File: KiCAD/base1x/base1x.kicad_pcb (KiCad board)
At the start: 4 copper layers, 62.2 x 110 mm, 39 parts, among them J1 Conn_02x05_Odd_Even, J2 GS3, J3 Conn_02x14_Counter_Clockwise, J4 GS3, J6 Conn_02x14_Counter_Clockwise, J7 Conn_02x06_Counter_Clockwise, J8 Conn_02x06_Counter_Clockwise, J9 Screw_Terminal_01x08, P3 CONN_01X02, P4 CONN_01X02, U1 ADS1115

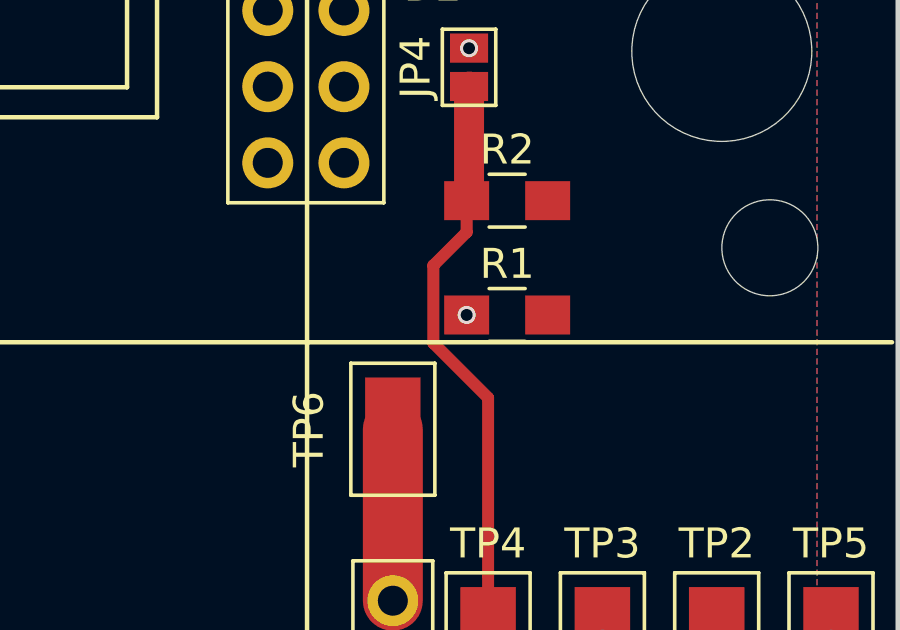
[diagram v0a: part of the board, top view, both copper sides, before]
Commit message: fix some clearance issues on base1x
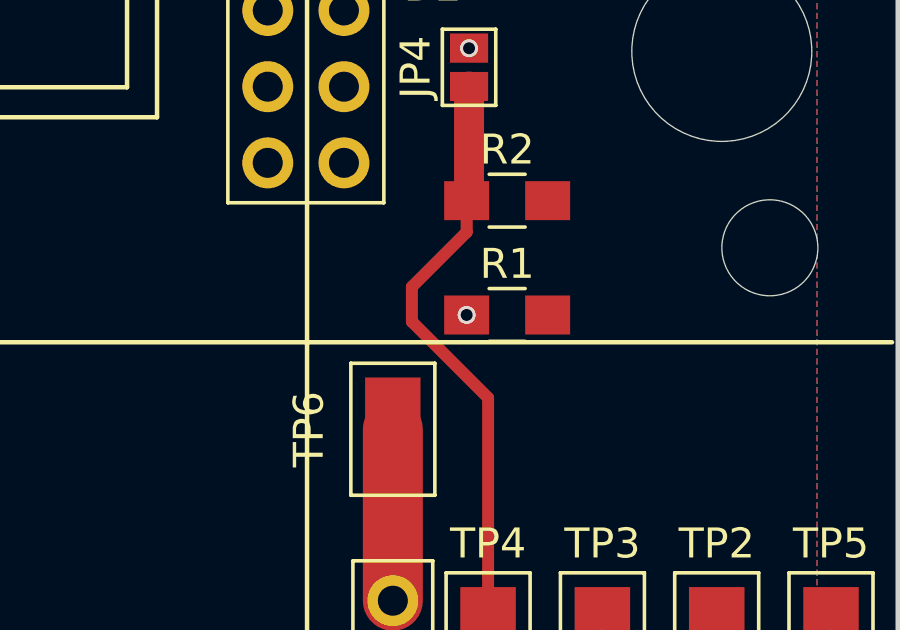
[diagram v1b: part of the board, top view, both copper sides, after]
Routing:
- net Net-(JP4-Pad1): track 26.3 -> 26.8 mm
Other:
- net class Default: clearance 0.16 -> 0.17
- rule trace_clearance: 0.16 -> 0.17
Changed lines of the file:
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@@
     (thickness 1.6)
     (drawings 27)
-    (tracks 210)
+    (tracks 214)
     (zones 0)
     (modules 39)
@@
     (user_trace_width 1)
     (user_trace_width 2)
-    (trace_clearance 0.16)
+    (trace_clearance 0.17)
     (zone_clearance 0.17)
     (zone_45_only no)
@@
   (net 28 "Net-(D2-Pad2)")
   (net_class Default "This is the default net class."
-    (clearance 0.16)
+    (clearance 0.17)
     (trace_width 0.25)
     (via_dia 0.6)
@@
   (segment (start -21.27 -1.26) (end -18.73 -1.26) (width 1) (layer In1.Cu) (net 1))
   (segment (start 21.23 -1.26) (end 18.69 -1.26) (width 1) (layer In1.Cu) (net 1))
+  (segment (start -8.075736 5.020001) (end -8.065736 5.030001) (width 0.4) (layer In1.Cu) (net 3))
+  (segment (start -8.5 5.020001) (end -8.075736 5.020001) (width 0.4) (layer In1.Cu) (net 3))
+  (segment (start -8.065736 5.030001) (end 17.479999 5.030001) (width 0.4) (layer In1.Cu) (net 3))
+  (segment (start 17.479999 5.030001) (end 17.840001 4.669999) (width 0.4) (layer In1.Cu) (net 3))
+  (segment (start 17.840001 4.669999) (end 18.69 3.82) (width 0.4) (layer In1.Cu) (net 3))
+  (segment (start -4.680001 -47.231997) (end -4.680001 -49.579999) (width 0.4) (layer In2.Cu) (net 4))
+  (segment (start -4.680001 -49.579999) (end -4.309999 -49.950001) (width 0.4) (layer In2.Cu) (net 4))
+  (segment (start -9.525 -42.386998) (end -4.680001 -47.231997) (width 0.4) (layer In2.Cu) (net 4))
+  (segment (start -4.309999 -49.950001) (end -3.46 -50.8) (width 0.4) (layer In2.Cu) (net 4))
   (segment (start -9.525 1.27) (end -9.525 -42.386998) (width 0.4) (layer In2.Cu) (net 4))
-  (segment (start -9.525 -42.386998) (end -9.366998 -42.545) (width 0.4) (layer In2.Cu) (net 4))
   (segment (start 18.69 1.28) (end -9.535 1.28) (width 1) (layer In1.Cu) (net 4))
   (segment (start -9.535 1.28) (end -9.525 1.27) (width 1) (layer In1.Cu) (net 4))
@@
   (segment (start -21.27 1.28) (end -18.73 1.28) (width 1) (layer In1.Cu) (net 4))
   (segment (start 21.23 1.28) (end 18.69 1.28) (width 1) (layer In1.Cu) (net 4))
+  (segment (start 27.305 25.4) (end 23.495 21.59) (width 0.4) (layer In2.Cu) (net 6))
+  (segment (start 27.305 38.1) (end 27.305 25.4) (width 0.4) (layer In2.Cu) (net 6))
+  (segment (start 22.079999 -8.030001) (end 21.23 -8.88) (width 0.4) (layer In2.Cu) (net 6))
+  (segment (start 23.495 21.59) (end 23.495 -6.615) (width 0.4) (layer In2.Cu) (net 6))
+  (segment (start 23.495 -6.615) (end 22.079999 -8.030001) (width 0.4) (layer In2.Cu) (net 6))
+  (segment (start 1.62 -9.165) (end 1.905 -8.88) (width 0.4) (layer In2.Cu) (net 6))
+  (segment (start 1.62 -48.26) (end 1.62 -9.165) (width 0.4) (layer In2.Cu) (net 6))
+  (segment (start 2.840001 -13.054999) (end 2.840001 -49.579999) (width 0.4) (layer In2.Cu) (net 7))
+  (segment (start 2.830001 -13.044999) (end 2.840001 -13.054999) (width 0.4) (layer In2.Cu) (net 7))
+  (segment (start 2.469999 -49.950001) (end 1.62 -50.8) (width 0.4) (layer In2.Cu) (net 7))
+  (segment (start 2.840001 -49.579999) (end 2.469999 -49.950001) (width 0.4) (layer In2.Cu) (net 7))
   (segment (start 8.255 -5.08) (end -7.64 -5.08) (width 0.4) (layer In1.Cu) (net 7))
   (segment (start -7.64 -5.08) (end -8.9 -6.34) (width 0.4) (layer In1.Cu) (net 7))
@@
   (segment (start -8.255 4.350737) (end -8.5 4.595737) (width 0.4) (layer In2.Cu) (net 3))
   (segment (start -8.5 4.595737) (end -8.5 5.020001) (width 0.4) (layer In2.Cu) (net 3))
-  (segment (start -3.46 -50.8) (end -4.789999 -49.470001) (width 0.4) (layer In2.Cu) (net 4))
-  (segment (start -4.789999 -49.470001) (end -4.789999 -47.121999) (width 0.4) (layer In2.Cu) (net 4))
-  (segment (start -4.789999 -47.121999) (end -9.366998 -42.545) (width 0.4) (layer In2.Cu) (net 4))
   (via (at 30.48 50.8) (size 0.6) (drill 0.4) (layers F.Cu B.Cu) (net 5))
   (via (at 31.75 50.8) (size 0.6) (drill 0.4) (layers F.Cu B.Cu) (net 5))
@@
   (segment (start 31.115 37.465) (end 29.55 37.465) (width 0.25) (layer F.Cu) (net 2))
   (via (at 31.115 37.465) (size 0.6) (drill 0.4) (layers F.Cu B.Cu) (net 2))
-  (segment (start 23.495 -6.615) (end 22.079999 -8.030001) (width 0.4) (layer In2.Cu) (net 6))
-  (segment (start 23.495 20.981238) (end 23.495 -6.615) (width 0.4) (layer In2.Cu) (net 6))
-  (segment (start 27.305 24.791238) (end 23.495 20.981238) (width 0.4) (layer In2.Cu) (net 6))
-  (segment (start 27.305 38.1) (end 27.305 24.791238) (width 0.4) (layer In2.Cu) (net 6))
-  (segment (start 22.079999 -8.030001) (end 21.23 -8.88) (width 0.4) (layer In2.Cu) (net 6))
   (segment (start 29.55 37.965) (end 27.44 37.965) (width 0.25) (layer F.Cu) (net 6))
   (segment (start 27.44 37.965) (end 27.305 38.1) (width 0.25) (layer F.Cu) (net 6))
@@
   (segment (start 29.55 36.465) (end 29.55 32.68) (width 0.25) (layer F.Cu) (net 16))
   (segment (start 29.55 32.68) (end 29.845 32.385) (width 0.25) (layer F.Cu) (net 16))
+  (segment (start 25.32 18.83) (end 23.495 20.655) (width 0.4) (layer F.Cu) (net 17))
+  (segment (start 23.495 21.813002) (end 26.035 24.353002) (width 0.4) (layer F.Cu) (net 17))
+  (segment (start 26.035 30.26) (end 26.035 32.385) (width 0.4) (layer F.Cu) (net 17))
   (segment (start 25.32 17.78) (end 25.32 18.83) (width 0.4) (layer F.Cu) (net 17))
-  (segment (start 25.32 18.83) (end 24.209999 19.940001) (width 0.4) (layer F.Cu) (net 17))
-  (segment (start 24.209999 19.940001) (end 24.209999 22.528001) (width 0.4) (layer F.Cu) (net 17))
-  (segment (start 24.209999 22.528001) (end 26.035 24.353002) (width 0.4) (layer F.Cu) (net 17))
+  (segment (start 23.495 20.655) (end 23.495 21.813002) (width 0.4) (layer F.Cu) (net 17))
   (segment (start 26.035 24.353002) (end 26.035 30.26) (width 0.4) (layer F.Cu) (net 17))
-  (segment (start 26.035 30.26) (end 26.035 32.385) (width 0.4) (layer F.Cu) (net 17))
   (segment (start 25.4 13.975) (end 25.4 17.7) (width 1) (layer F.Cu) (net 17))
   (segment (start 25.4 17.7) (end 25.32 17.78) (width 1) (layer F.Cu) (net 17))
@@
   (segment (start 1.905 -8.88) (end -18.73 -8.88) (width 1) (layer In1.Cu) (net 6))
   (segment (start 18.69 -8.88) (end 1.905 -8.88) (width 1) (layer In1.Cu) (net 6))
-  (segment (start 1.62 -50.8) (end 2.830001 -49.589999) (width 0.4) (layer In2.Cu) (net 7))
-  (segment (start 2.830001 -49.589999) (end 2.830001 -13.044999) (width 0.4) (layer In2.Cu) (net 7))
-  (segment (start 1.62 -48.26) (end 1.62 -9.165) (width 0.4) (layer In2.Cu) (net 6))
-  (segment (start 1.62 -9.165) (end 1.905 -8.88) (width 0.4) (layer In2.Cu) (net 6))
   (via (at 1.905 -8.88) (size 0.6) (drill 0.4) (layers F.Cu B.Cu) (net 6))
   (segment (start 22.86 25.4) (end 22.86 31.115) (width 2) (layer F.Cu) (net 12))
@@
   (segment (start -18.73 -16.5) (end -21.27 -16.5) (width 2) (layer F.Cu) (net 2))
   (segment (start -8.5 5.020001) (end -17.529999 5.020001) (width 0.4) (layer In1.Cu) (net 3))
-  (segment (start -8.5 5.020001) (end 17.489999 5.020001) (width 0.4) (layer In1.Cu) (net 3))
   (via (at -8.5 5.020001) (size 0.6) (drill 0.4) (layers F.Cu B.Cu) (net 3))
   (via (at 35.75 6.25) (size 0.6) (drill 0.4) (layers F.Cu B.Cu) (net 5))
@@
   (segment (start 18.69 3.82) (end 21.23 3.82) (width 0.4) (layer In1.Cu) (net 3))
   (segment (start -18.73 3.82) (end -17.529999 5.020001) (width 0.4) (layer In1.Cu) (net 3))
-  (segment (start 17.489999 5.020001) (end 17.840001 4.669999) (width 0.4) (layer In1.Cu) (net 3))
-  (segment (start 17.840001 4.669999) (end 18.69 3.82) (width 0.4) (layer In1.Cu) (net 3))
   (segment (start -21.27 3.82) (end -18.73 3.82) (width 0.4) (layer In1.Cu) (net 3))
   (segment (start -21.27 6.36) (end -18.73 6.36) (width 1) (layer B.Cu) (net 5))

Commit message: update silk
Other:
- board text added: "b2641be"
- board text removed: "3ec2e93"
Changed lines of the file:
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@@
       (xy 8.293997 0.976563) (xy 8.491005 0.779554)) (layer F.SilkS) (width 0.001))
   )
-  (gr_text 3ec2e93 (at 13.335 43.18) (layer F.SilkS)
+  (gr_text b2641be (at 13.335 43.18) (layer F.SilkS)
     (effects (font (size 1.5 1.5) (thickness 0.3)))
   )

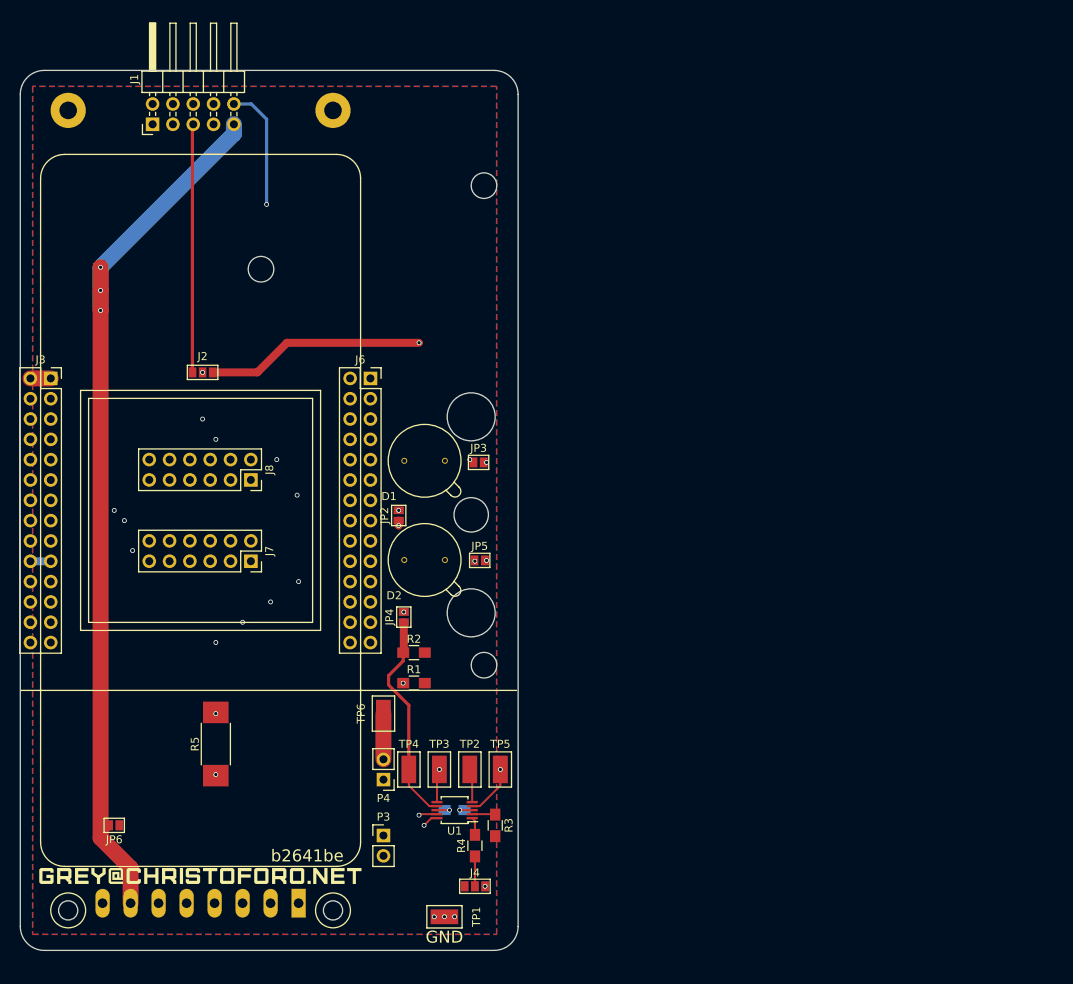
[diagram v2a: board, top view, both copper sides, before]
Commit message: starting on ethercat board pin boards rotated base1x zones fixed
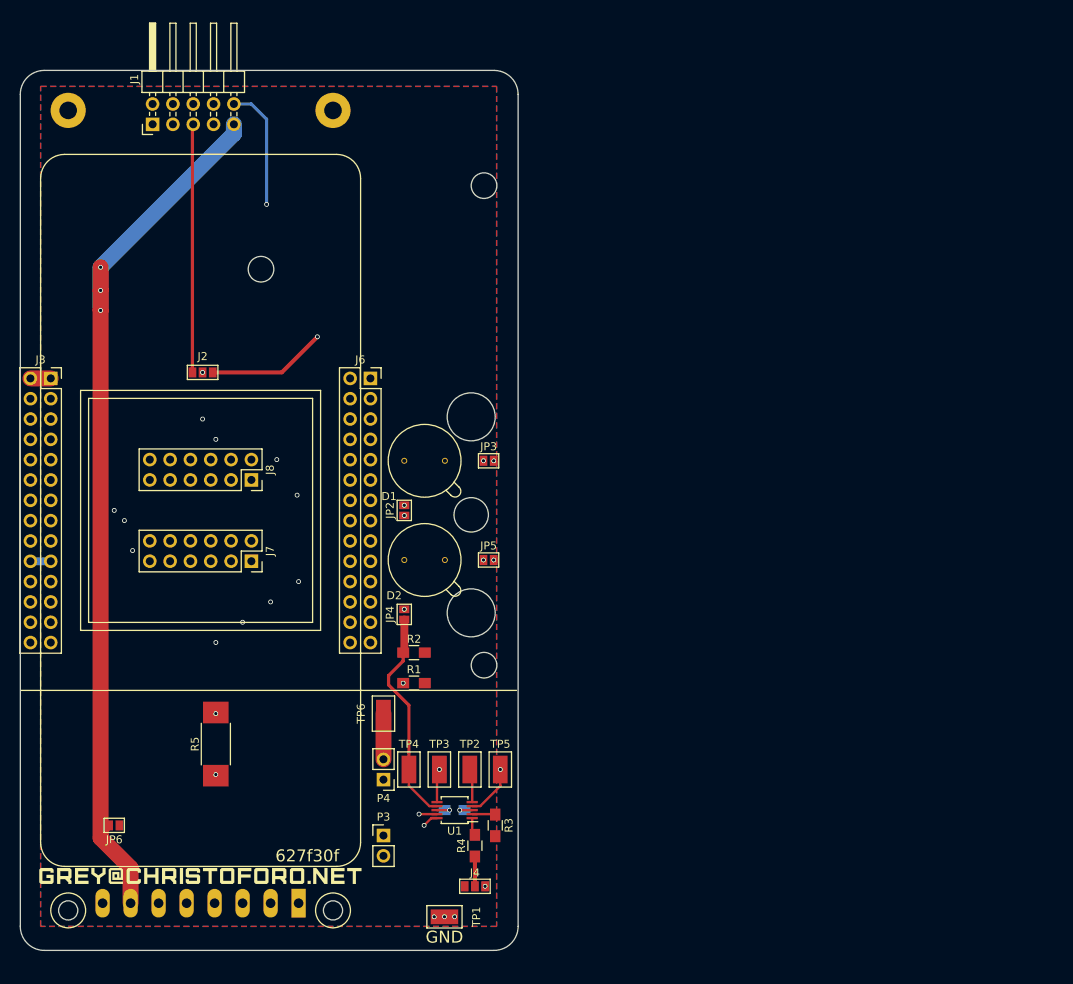
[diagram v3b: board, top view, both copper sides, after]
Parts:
- moved JP3 1.27 mm to (36.0, -6.20)
- moved JP5 1.11 mm to (36.0, 6.20)
- moved JP2 0.94 mm to (25.5, 0.00)
- moved JP4 0.34 mm to (25.5, 13.0)
- moved J7 0.07 mm to (6.35, 6.35)
- moved J8 0.07 mm to (6.35, -3.81)
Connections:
- J3 pad 12: (no net) -> /~CSL
- J3 pad 22: (no net) -> /I+L
- J3 pad 24: (no net) -> /V+L
- J3 pad 26: (no net) -> /V-L
- J3 pad 28: (no net) -> /I-L
- J6 pad 11: (no net) -> /~CSR
- J6 pad 21: (no net) -> /I+R
- J6 pad 23: (no net) -> /V+R
- J6 pad 25: (no net) -> /V-R
- J6 pad 27: (no net) -> /I-R
- J7 pad 1: (no net) -> Net-(J7-Pad1)
- J7 pad 10: (no net) -> Net-(J7-Pad10)
- J7 pad 11: (no net) -> Net-(J7-Pad11)
- J7 pad 12: (no net) -> Net-(J7-Pad12)
- J7 pad 2: (no net) -> Net-(J7-Pad2)
- J7 pad 3: (no net) -> Net-(J7-Pad3)
- J7 pad 4: (no net) -> Net-(J7-Pad4)
- J7 pad 5: (no net) -> Net-(J7-Pad5)
- J7 pad 6: (no net) -> Net-(J7-Pad6)
- J7 pad 7: (no net) -> Net-(J7-Pad7)
- J7 pad 8: (no net) -> Net-(J7-Pad8)
- J7 pad 9: (no net) -> Net-(J7-Pad9)
- J8 pad 1: (no net) -> Net-(J8-Pad1)
- J8 pad 10: (no net) -> Net-(J8-Pad10)
- J8 pad 11: (no net) -> Net-(J8-Pad11)
- J8 pad 12: (no net) -> Net-(J8-Pad12)
- J8 pad 2: (no net) -> Net-(J8-Pad2)
- J8 pad 3: (no net) -> Net-(J8-Pad3)
- J8 pad 4: (no net) -> Net-(J8-Pad4)
- J8 pad 5: (no net) -> Net-(J8-Pad5)
- J8 pad 6: (no net) -> Net-(J8-Pad6)
- J8 pad 7: (no net) -> Net-(J8-Pad7)
- J8 pad 8: (no net) -> Net-(J8-Pad8)
- J8 pad 9: (no net) -> Net-(J8-Pad9)
- J9 pad 6: (no net) -> Net-(J9-Pad6)
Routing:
- net Net-(D1-Pad2): track 3.18 -> 4.82 mm
- net V_D_LOC: track 92.2 -> 90.7 mm
- net Net-(D2-Pad2): track 3.81 -> 4.82 mm
- net Net-(D1-Pad1): track 6.49 -> 5.56 mm
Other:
- net class Default: clearance 0.17 -> 0.16
- rule trace_clearance: 0.17 -> 0.16
- board text added: "627f30f"
- board text removed: "b2641be"

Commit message: update silk
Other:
- board text added: "20b2bb8"
- board text removed: "627f30f"
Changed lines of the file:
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@@
       (xy 18.001028 -0.623664) (xy 18.001028 -1.023438) (xy 16.304893 -1.023438) (xy 16.304893 0.976563)) (layer F.SilkS) (width 0.001))
   )
-  (gr_text 627f30f (at 13.335 43.18) (layer F.SilkS)
+  (gr_text 20b2bb8 (at 13.335 43.18) (layer F.SilkS)
     (effects (font (size 1.5 1.5) (thickness 0.3)))
   )
